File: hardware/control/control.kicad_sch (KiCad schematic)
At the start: 59 parts, among them J1 Conn_01x05_Male, J2 DCDC-PWM, J3 display, J4 DCDC-MEASURES, J5 CANPWR, J6 CANGND, J7 RJ45, J8 RJ45, J9 Conn_02x03_Odd_Even, Q1 BSS123, SW1 next, SW2 select, U1 2.048V, U2 AP63200WU, U3 PIC18F27Q84, U4 TLE9250VSJXUMA1, Y1 10Mhz

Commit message: Final pass on part numbers
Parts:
- C1, C12, C14, C5, C8: P/N MC0603B104K250CT -> MC0603B104K250CT (stock)
- C10: P/N (none) -> MC0805B101K500CT (F)
- C11, C13: P/N CL31A226KAHNNN -> CL31A226KAHNNN (M)
- C15: P/N NFM21PC104R1E3D -> NFM21PC104R1E3D (M)
- C2, C3: P/N GRM31CR71H475KA12L -> GRM31CR71H475KA12L (M)
- C4, C9: P/N C1206C104K5RACTU -> C1206C104K5RACTU (M)
- C6, C7, J5, J6: P/N (none) -> stock
- D3: P/N (none) -> SMBJ16Ae3/TR13 (M)
- F1, F2: P/N MC011014 -> MC011014 (F)
- H1, H2, H3, H4: P/N (none) -> N/A
- J2, J4: P/N DW-05-15-T-D-250 -> DW-05-15-T-D-250 (M)
- J3: P/N M20-7810345 -> M20-7810345 (M)
- L1: P/N MP002847 -> MP002847 (F)
- R1: P/N (none) -> WF08P2703FTL (F)
- R13: P/N (none) -> WF08P1003FTL (F)
- R16: P/N (none) -> WF08P2202FTL (F)
- R2, R6: P/N (none) -> MCWR08X3002FTL (F)
- R5: P/N (none) -> CR0805-FX-1583ELF (M)
- R9: P/N (none) -> MFR3-8K2FC (F)
- SW1, SW2: P/N D6R -> D6R90LFS (F)
- U2: P/N AP63200WU -> AP63200WU-7 (M)
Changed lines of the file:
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@@
+      (effects (font (size 1.27 1.27)) hide)
+    )
+    (property "P/N" "N/A" (id 4) (at 254.635 88.265 0)
       (effects (font (size 1.27 1.27)) hide)
     )
@@
       (effects (font (size 1.27 1.27)) hide)
     )
+    (property "P/N" "N/A" (id 4) (at 254.635 95.885 0)
+      (effects (font (size 1.27 1.27)) hide)
+    )
     (pin "1")
   )
@@
       (effects (font (size 1.27 1.27)) hide)
     )
+    (property "P/N" "N/A" (id 4) (at 254.635 103.505 0)
+      (effects (font (size 1.27 1.27)) hide)
+    )
     (pin "1")
   )
@@
       (effects (font (size 1.27 1.27)) hide)
     )
+    (property "P/N" "N/A" (id 4) (at 254.635 111.125 0)
+      (effects (font (size 1.27 1.27)) hide)
+    )
     (pin "1")
   )
@@
       (effects (font (size 1.27 1.27)) hide)
     )
-    (property "P/N" "MC0603B104K250CT" (id 4) (at 36.83 54.61 0)
+    (property "P/N" "MC0603B104K250CT (stock)" (id 4) (at 36.83 54.61 0)
       (effects (font (size 1.27 1.27)) hide)
     )
@@
       (effects (font (size 1.27 1.27)) hide)
     )
-    (property "P/N" "MC011014" (id 4) (at 63.5 115.57 0)
+    (property "P/N" "MC011014 (F)" (id 4) (at 63.5 115.57 0)
       (effects (font (size 1.27 1.27)) hide)
     )
@@
       (effects (font (size 1.27 1.27)) hide)
     )
-    (property "P/N" "MC0603B104K250CT" (id 4) (at 27.94 74.93 0)
+    (property "P/N" "MC0603B104K250CT (stock)" (id 4) (at 27.94 74.93 0)
       (effects (font (size 1.27 1.27)) hide)
     )
@@
       (effects (font (size 1.27 1.27)) hide)
     )
+    (property "P/N" "MCWR08X3002FTL (F)" (id 4) (at 69.85 167.005 0)
+      (effects (font (size 1.27 1.27)) hide)
+    )
     (pin "1")
     (pin "2")
@@
       (effects (font (size 1.27 1.27)) hide)
     )
-    (property "P/N" "GRM31CR71H475KA12L" (id 4) (at 30.48 136.525 0)
+    (property "P/N" "GRM31CR71H475KA12L (M)" (id 4) (at 30.48 136.525 0)
       (effects (font (size 1.27 1.27)) hide)
     )
@@
       (effects (font (size 1.27 1.27)) hide)
     )
+    (property "P/N" "WF08P2202FTL (F)" (id 4) (at 198.12 142.24 0)
+      (effects (font (size 1.27 1.27)) hide)
+    )
     (pin "1")
     (pin "2")
@@
     )
     (property "Datasheet" "~" (id 3) (at 76.2 159.385 0)
+      (effects (font (size 1.27 1.27)) hide)
+    )
+    (property "P/N" "MC0805B101K500CT (F)" (id 4) (at 76.2 159.385 0)
       (effects (font (size 1.27 1.27)) hide)
     )
@@
       (effects (font (size 1.27 1.27)) hide)
     )
-    (property "P/N" "C1206C104K5RACTU" (id 4) (at 59.69 158.115 0)
+    (property "P/N" "C1206C104K5RACTU (M)" (id 4) (at 59.69 158.115 0)
       (effects (font (size 1.27 1.27)) hide)
     )
@@
       (effects (font (size 1.27 1.27)) hide)
     )
+    (property "P/N" "CR0805-FX-1583ELF (M)" (id 4) (at 69.85 159.385 0)
+      (effects (font (size 1.27 1.27)) hide)
+    )
     (pin "1")
     (pin "2")
@@
     )
     (property "Datasheet" "~" (id 3) (at 46.99 73.66 0)
+      (effects (font (size 1.27 1.27)) hide)
+    )
+    (property "P/N" "stock" (id 4) (at 46.99 73.66 0)
       (effects (font (size 1.27 1.27)) hide)
     )
@@
       (effects (font (size 1.27 1.27)) hide)
     )
-    (property "P/N" "AP63200WU" (id 4) (at 44.45 158.115 0)
+    (property "P/N" "AP63200WU-7 (M)" (id 4) (at 44.45 158.115 0)
       (effects (font (size 1.27 1.27)) hide)
     )
@@
       (effects (font (size 1.27 1.27)) hide)
     )
-    (property "P/N" "MC0603B104K250CT" (id 4) (at 87.63 31.75 0)
+    (property "P/N" "MC0603B104K250CT (stock)" (id 4) (at 87.63 31.75 0)
       (effects (font (size 1.27 1.27)) hide)
     )
@@
       (effects (font (size 1.27 1.27)) hide)
     )
-    (property "P/N" "CL31A226KAHNNN" (id 4) (at 83.82 159.385 0)
+    (property "P/N" "CL31A226KAHNNN (M)" (id 4) (at 83.82 159.385 0)
       (effects (font (size 1.27 1.27)) hide)
     )
@@
       (effects (font (size 1.27 1.27)) hide)
     )
-    (property "P/N" "NFM21PC104R1E3D" (id 4) (at 194.31 54.61 0)
+    (property "P/N" "NFM21PC104R1E3D (M)" (id 4) (at 194.31 54.61 0)
       (effects (font (size 1.27 1.27)) hide)
     )
@@
     )
     (property "Datasheet" "~" (id 3) (at 46.99 68.58 0)
+      (effects (font (size 1.27 1.27)) hide)
+    )
+    (property "P/N" "stock" (id 4) (at 46.99 68.58 0)
       (effects (font (size 1.27 1.27)) hide)
     )
@@
       (effects (font (size 1.27 1.27)) hide)
     )
-    (property "P/N" "MP002847" (id 4) (at 66.04 155.575 0)
+    (property "P/N" "MP002847 (F)" (id 4) (at 66.04 155.575 0)
       (effects (font (size 1.27 1.27)) hide)
     )
@@
       (effects (font (size 1.27 1.27)) hide)
     )
-    (property "P/N" "CL31A226KAHNNN" (id 4) (at 90.17 159.385 0)
+    (property "P/N" "CL31A226KAHNNN (M)" (id 4) (at 90.17 159.385 0)
       (effects (font (size 1.27 1.27)) hide)
     )
@@
     )
     (property "Datasheet" "~" (id 3) (at 176.53 44.45 0)
+      (effects (font (size 1.27 1.27)) hide)
+    )
+    (property "P/N" "stock" (id 4) (at 176.53 44.45 0)
       (effects (font (size 1.27 1.27)) hide)
     )
@@
       (effects (font (size 1.27 1.27)) hide)
     )
-    (property "P/N" "MC011014" (id 4) (at 63.5 124.46 0)
+    (property "P/N" "MC011014 (F)" (id 4) (at 63.5 124.46 0)
       (effects (font (size 1.27 1.27)) hide)
     )
@@
       (effects (font (size 1.27 1.27)) hide)
     )
-    (property "P/N" "M20-7810345" (id 4) (at 144.78 142.24 0)
+    (property "P/N" "M20-7810345 (M)" (id 4) (at 144.78 142.24 0)
       (effects (font (size 1.27 1.27)) hide)
     )
@@
       (effects (font (size 1.27 1.27)) hide)
     )
-    (property "P/N" "DW-05-15-T-D-250" (id 4) (at 114.3 110.49 0)
+    (property "P/N" "DW-05-15-T-D-250 (M)" (id 4) (at 114.3 110.49 0)
       (effects (font (size 1.27 1.27)) hide)
     )
@@
       (effects (font (size 1.27 1.27)) hide)
     )
-    (property "P/N" "DW-05-15-T-D-250" (id 4) (at 153.67 105.41 0)
+    (property "P/N" "DW-05-15-T-D-250 (M)" (id 4) (at 153.67 105.41 0)
       (effects (font (size 1.27 1.27)) hide)
     )
@@
       (effects (font (size 1.27 1.27)) hide)
     )
-    (property "P/N" "GRM31CR71H475KA12L" (id 4) (at 30.48 128.905 0)
+    (property "P/N" "GRM31CR71H475KA12L (M)" (id 4) (at 30.48 128.905 0)
       (effects (font (size 1.27 1.27)) hide)
     )
@@
       (effects (font (size 1.27 1.27)) hide)
     )
-    (property "P/N" "MC0603B104K250CT" (id 4) (at 58.42 82.55 0)
+    (property "P/N" "MC0603B104K250CT (stock)" (id 4) (at 58.42 82.55 0)
       (effects (font (size 1.27 1.27)) hide)
     )
@@
     )
     (property "Datasheet" "~" (id 3) (at 24.13 167.005 0)
+      (effects (font (size 1.27 1.27)) hide)
+    )
+    (property "P/N" "MCWR08X3002FTL (F)" (id 4) (at 24.13 167.005 0)
       (effects (font (size 1.27 1.27)) hide)
     )
@@
       (effects (font (size 1.27 1.27)) hide)
     )
-    (property "P/N" "D6R" (id 4) (at 207.01 142.24 0)
+    (property "P/N" "D6R90LFS (F)" (id 4) (at 207.01 142.24 0)
       (effects (font (size 1.27 1.27)) hide)
     )
@@
     )
     (property "Datasheet" "~" (id 3) (at 184.15 92.71 0)
+      (effects (font (size 1.27 1.27)) hide)
+    )
+    (property "P/N" "WF08P1003FTL (F)" (id 4) (at 184.15 92.71 0)
       (effects (font (size 1.27 1.27)) hide)
     )
@@
       (effects (font (size 1.27 1.27)) hide)
     )
-    (property "P/N" "C1206C104K5RACTU" (id 4) (at 30.48 145.415 0)
+    (property "P/N" "C1206C104K5RACTU (M)" (id 4) (at 30.48 145.415 0)
       (effects (font (size 1.27 1.27)) hide)
     )
@@
       (effects (font (size 1.27 1.27)) hide)
     )
+    (property "P/N" "MFR3-8K2FC (F)" (id 4) (at 105.41 87.63 0)
+      (effects (font (size 1.27 1.27)) hide)
+    )
     (pin "1")
     (pin "2")
@@
     )
     (property "Datasheet" "https://www.vishay.com/docs/88301/15ke.pdf" (id 3) (at 201.93 54.61 0)
+      (effects (font (size 1.27 1.27)) hide)
+    )
+    (property "P/N" " SMBJ16Ae3/TR13 (M)" (id 4) (at 201.93 53.34 0)
       (effects (font (size 1.27 1.27)) hide)
     )
@@
     )
     (property "Datasheet" "~" (id 3) (at 24.13 159.385 0)
+      (effects (font (size 1.27 1.27)) hide)
+    )
+    (property "P/N" "WF08P2703FTL (F)" (id 4) (at 24.13 159.385 0)
       (effects (font (size 1.27 1.27)) hide)
     )
@@
       (effects (font (size 1.27 1.27)) hide)
     )
-    (property "P/N" "D6R" (id 4) (at 207.01 127 0)
+    (property "P/N" "D6R90LFS (F)" (id 4) (at 207.01 127 0)
       (effects (font (size 1.27 1.27)) hide)
     )
@@
       (effects (font (size 1.27 1.27)) hide)
     )
+    (property "P/N" "stock" (id 4) (at 187.96 44.45 0)
+      (effects (font (size 1.27 1.27)) hide)
+    )
     (pin "1")
     (pin "2")
@@
       (effects (font (size 1.27 1.27)) hide)
     )
-    (property "P/N" "MC0603B104K250CT" (id 4) (at 151.13 46.99 0)
-      (effects (font (size 1.27 1.27)) hide)
-    )
+    (property "P/N" "MC0603B104K250CT (stock)" (id 4) (at 151.13 46.99 0)
+      (effects (font (size 1.27 1.27)) hide)
+    )

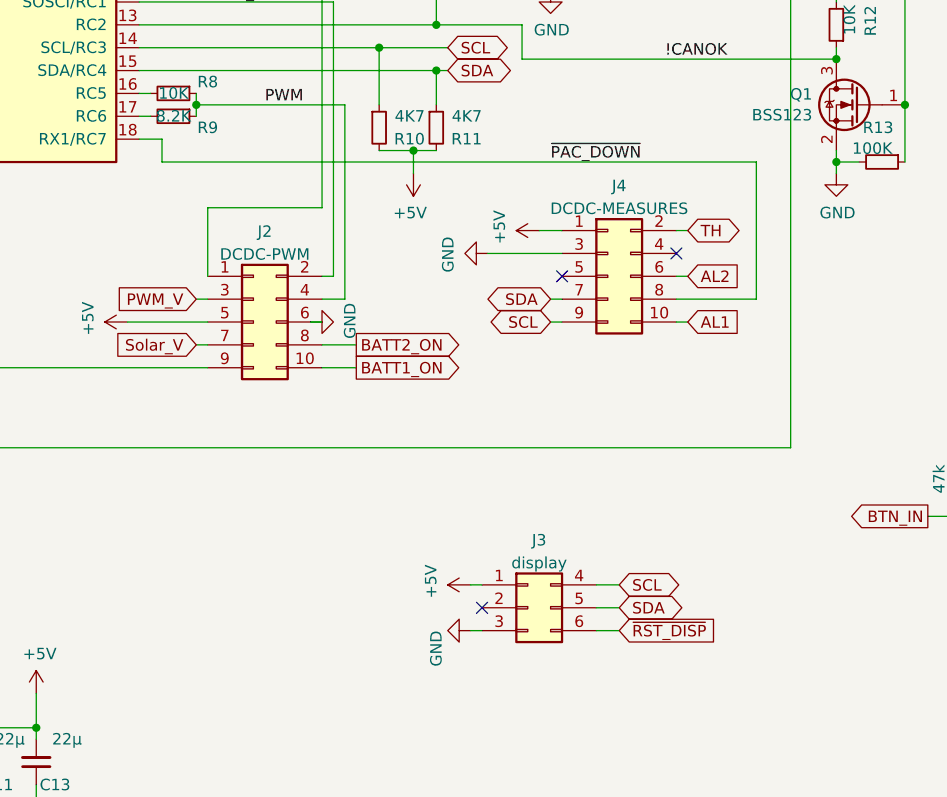
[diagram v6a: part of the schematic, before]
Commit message: *: connect unused connectors pins to GND
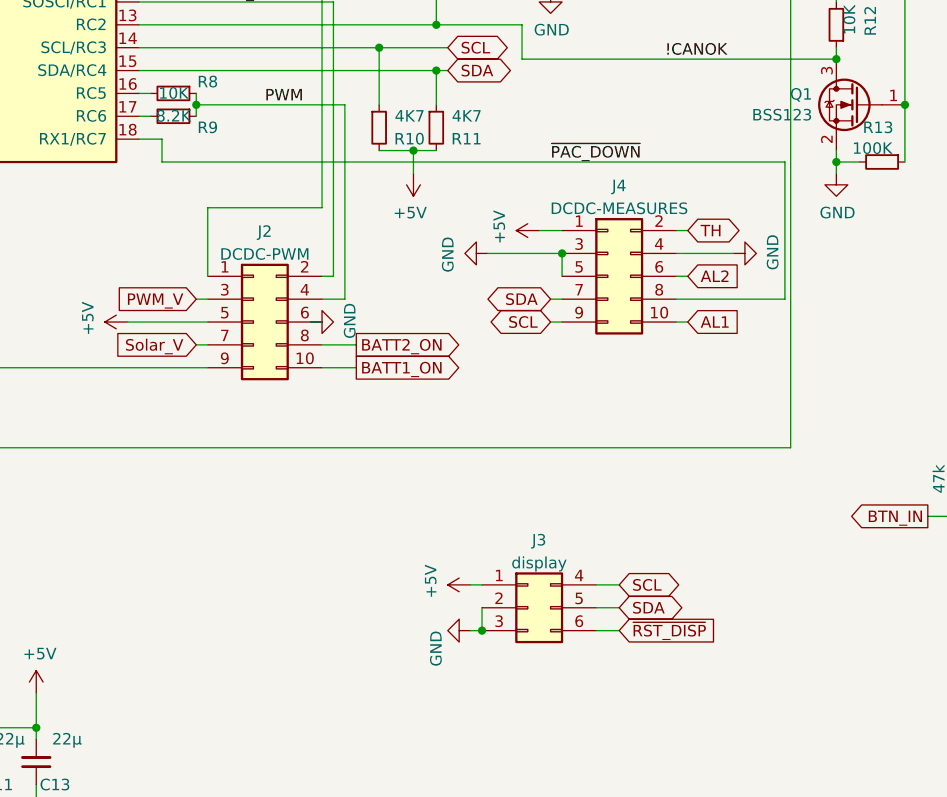
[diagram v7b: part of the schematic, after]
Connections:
- net GND: now also J3.2 (Pin_2), J4.4 (Pin_4), J4.5 (Pin_5)
- no-connect marks 7 -> 4
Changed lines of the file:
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@@
 (kicad_sch (version 20211123) (generator eeschema)
   (paper "A4")
+  (junction (at 148.59 102.87) (diameter 0) (color 0 0 0 0)
+  )
   (junction (at 207.01 49.53) (diameter 0) (color 0 0 0 0)
   )
@@
   )
   (junction (at 90.17 155.575) (diameter 0) (color 0 0 0 0)
+  )
+  (junction (at 139.7 144.78) (diameter 0) (color 0 0 0 0)
   )
   (junction (at 231.14 44.45) (diameter 0) (color 0 0 0 0)
@@
   (no_connect (at 212.09 127))
   (no_connect (at 201.93 127))
-  (no_connect (at 161.29 102.87))
-  (no_connect (at 148.59 105.41))
-  (no_connect (at 139.7 142.24))
   (wire (pts (xy 101.6 80.01) (xy 128.27 80.01))
     (stroke (width 0) (type default) (color 0 0 0 0))
@@
     (stroke (width 0) (type default) (color 0 0 0 0))
   )
+  (wire (pts (xy 148.59 102.87) (xy 148.59 105.41))
+    (stroke (width 0) (type default) (color 0 0 0 0))
+  )
   (wire (pts (xy 249.555 106.045) (xy 249.555 98.425))
     (stroke (width 0) (type default) (color 0 0 0 0))
@@
     (stroke (width 0) (type default) (color 0 0 0 0))
   )
-  (wire (pts (xy 170.18 107.95) (xy 161.29 107.95))
+  (wire (pts (xy 173.355 107.95) (xy 161.29 107.95))
     (stroke (width 0) (type default) (color 0 0 0 0))
   )
@@
     (stroke (width 0) (type default) (color 0 0 0 0))
   )
-  (wire (pts (xy 170.18 92.71) (xy 170.18 107.95))
+  (wire (pts (xy 173.355 92.71) (xy 173.355 107.95))
     (stroke (width 0) (type default) (color 0 0 0 0))
   )
@@
     (stroke (width 0) (type default) (color 0 0 0 0))
   )
+  (wire (pts (xy 161.29 102.87) (xy 167.64 102.87))
+    (stroke (width 0) (type default) (color 0 0 0 0))
+  )
   (wire (pts (xy 101.6 85.09) (xy 102.87 85.09))
     (stroke (width 0) (type default) (color 0 0 0 0))
@@
     (stroke (width 0) (type default) (color 0 0 0 0))
   )
+  (wire (pts (xy 139.7 142.24) (xy 139.7 144.78))
+    (stroke (width 0) (type default) (color 0 0 0 0))
+  )
   (wire (pts (xy 100.33 110.49) (xy 109.22 110.49))
     (stroke (width 0) (type default) (color 0 0 0 0))
@@
     (stroke (width 0) (type default) (color 0 0 0 0))
   )
-  (wire (pts (xy 104.14 92.71) (xy 170.18 92.71))
+  (wire (pts (xy 104.14 92.71) (xy 173.355 92.71))
     (stroke (width 0) (type default) (color 0 0 0 0))
   )
@@
     (pin "1")
   )
+  (symbol (lib_id "power:GND") (at 167.64 102.87 90) (unit 1)
+    (in_bom yes) (on_board yes)
+    (property "Reference" "#PWR?" (id 0) (at 173.99 102.87 0)
+      (effects (font (size 1.27 1.27)) hide)
+    )
+    (property "Value" "GND" (id 1) (at 172.0342 102.743 0))
+    (property "Footprint" "" (id 2) (at 167.64 102.87 0)
+      (effects (font (size 1.27 1.27)) hide)
+    )
+    (property "Datasheet" "" (id 3) (at 167.64 102.87 0)
+      (effects (font (size 1.27 1.27)) hide)
+    )
+    (pin "1")
+  )
   (symbol (lib_id "Switch:SW_Push_Dual") (at 207.01 127 0) (unit 1)
     (in_bom yes) (on_board yes) (fields_autoplaced)
@@
       (reference "#PWR0101") (unit 1) (value "GND") (footprint "")
     )
+    (path "/f65101fd-290c-4c96-8961-66fc9085d00a"
+      (reference "#PWR?") (unit 1) (value "GND") (footprint "")
+    )
     (path "/0c0222ff-2875-415e-9bf8-78a11b090087"
